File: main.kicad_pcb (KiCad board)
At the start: 2 copper layers, 228.6 x 70.6 mm, 133 parts, among them J1 Conn_02x16_Row_Letter_First, J10 Conn_01x26_Pin, J11 Conn_ARM_JTAG_SWD_10, J2 Conn_01x05, J3 Conn_01x02, J4 Screw_Terminal_01x02, J5 Screw_Terminal_01x10, J6 Screw_Terminal_01x10, J7 Screw_Terminal_01x02, J8 Screw_Terminal_01x10, J9 Screw_Terminal_01x10, U10 TLP3558A, U11 TLP3558A, U12 TLP3558A, U13 TLP3558A, U14 TLP3558A, U15 TLP3558A, U16 TLP3558A, U17 TLP3558A, U18 TLP3558A, U19 TLP3558A, U2 NCP1117-3.3_TO252, U20 TLP3558A, U21 TLP3558A, U22 TLP3558A, U23 TLP3558A, U24 TLP3558A, U25 TLP3558A, U26 TLP3558A, U27 TLP3558A, U28 TLP3558A, U29 TLP3558A, U3 STM32G070KBT6, U30 TLP3558A, U31 TLP3558A, U32 TLP3558A, U33 TLP3558A, U34 TLP3558A, U35 TLP3558A, U36 TLP3558A, U37 TLP3558A, U38 TLP3558A, U39 TLP3558A, U4 TLP3558A, U40 TLP3558A, U41 TLP3558A, U42 TLP3558A, U43 TLP3558A, U44 TLP3558A, U45 TLP3558A, U46 TLP3558A, U47 TLP3558A, U5 TLP3558A, U6 TLP3558A, U7 TLP3558A, U8 TLP3558A, U9 TLP3558A

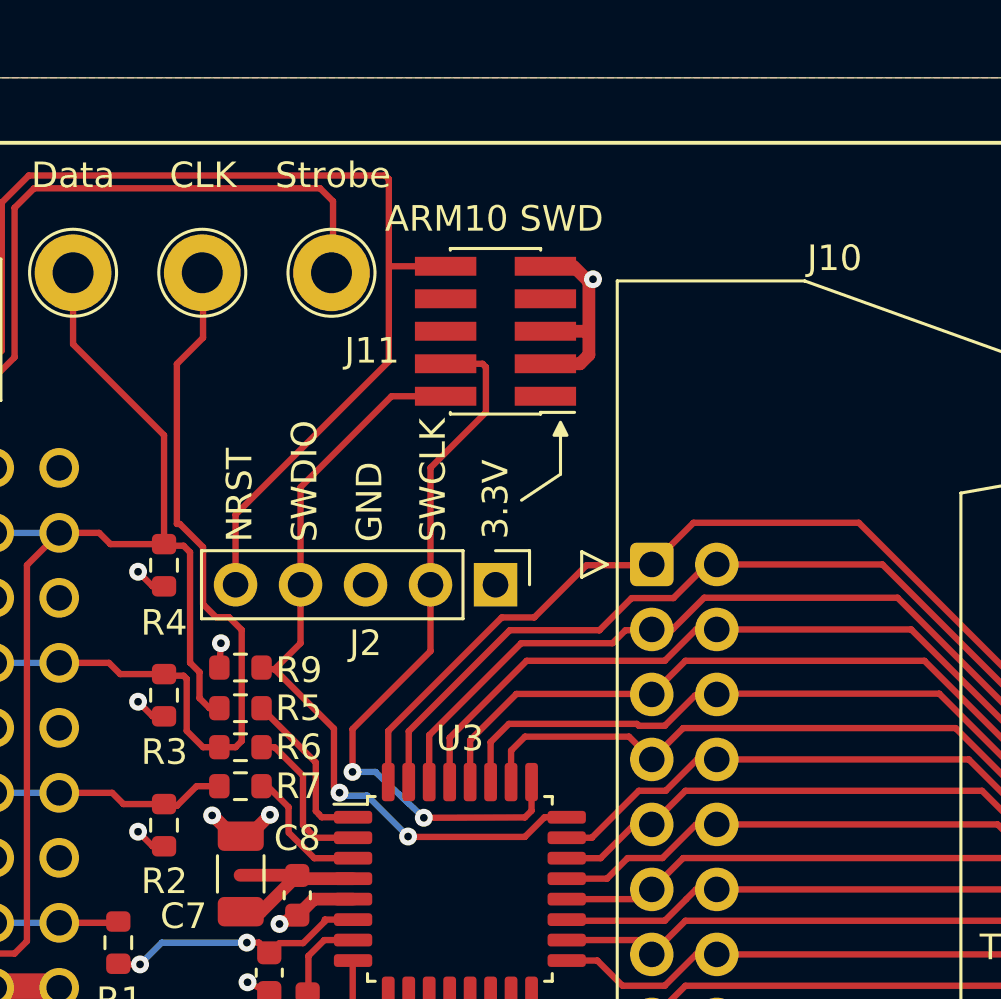
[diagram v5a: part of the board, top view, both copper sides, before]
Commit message: nicer SWD header
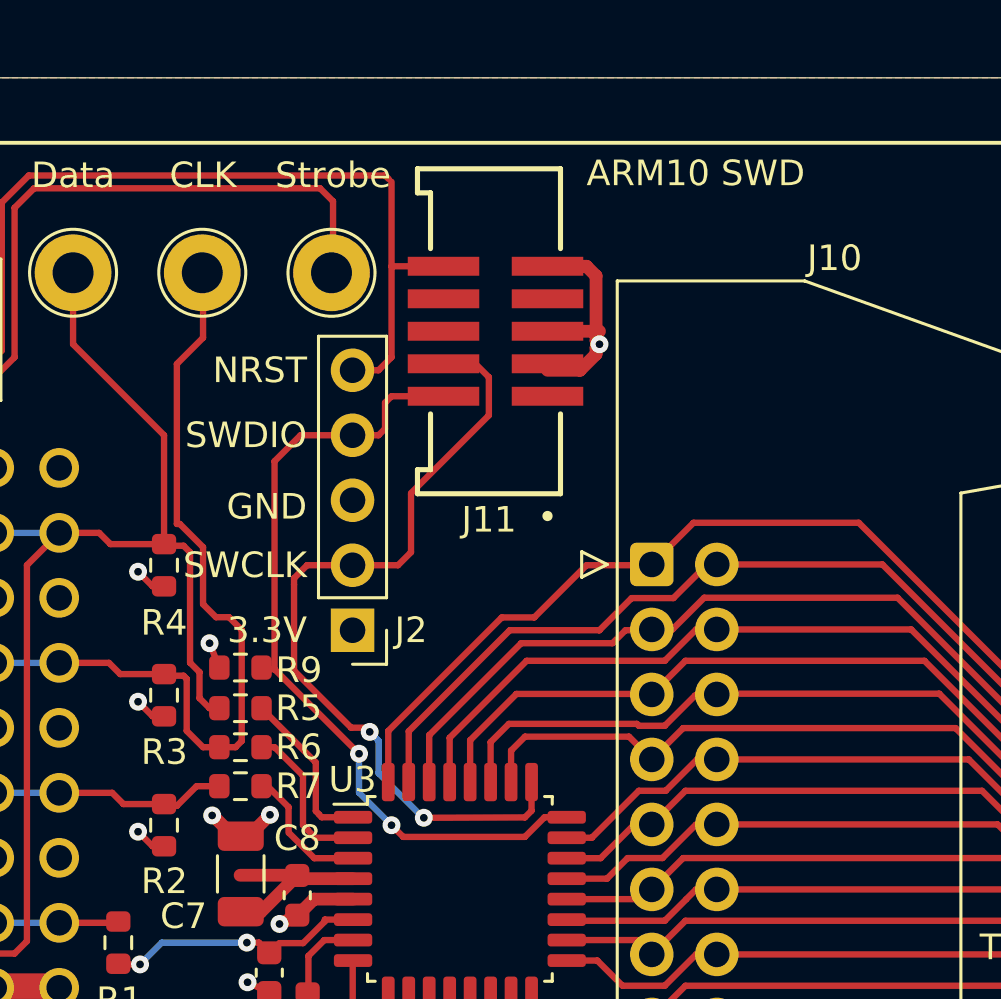
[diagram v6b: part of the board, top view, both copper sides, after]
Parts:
- J11: footprint Connector_PinHeader_1.27mm:PinHeader_2x05_P1.27mm_Vertical_SMD -> Custom_footprints_project:SAMTEC_SHF-105-01-L-D-SM-K-TR
- moved J2 5.86 mm to (44.7, 69.8), turned to 180 degrees
- turned J11 to 90 degrees
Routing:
- net /~{NRST}: track 70.2 -> 61.2 mm
- net /Microcontroller/SWCLK: track 28.6 -> 32.3 mm
- net GND: track 26.2 -> 28.4 mm

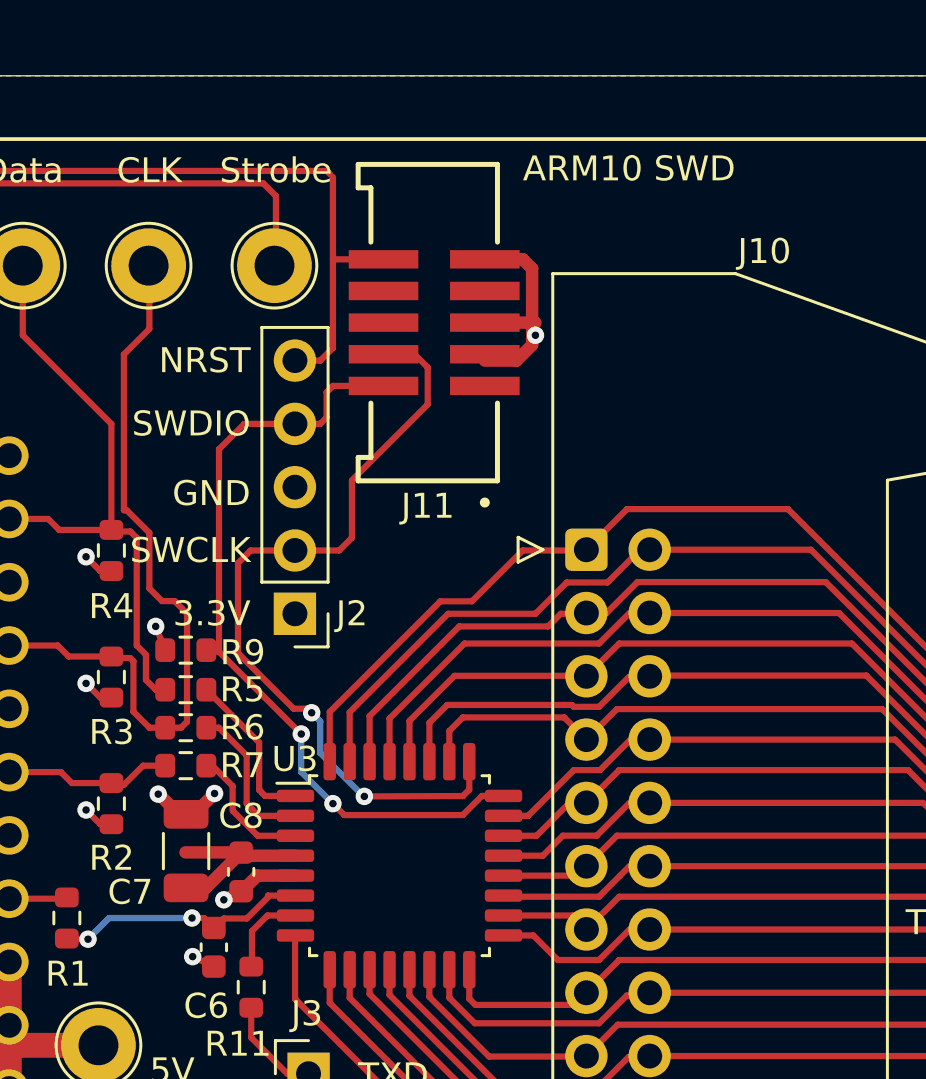
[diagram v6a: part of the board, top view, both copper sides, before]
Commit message: footprint of SWD connector more compatible
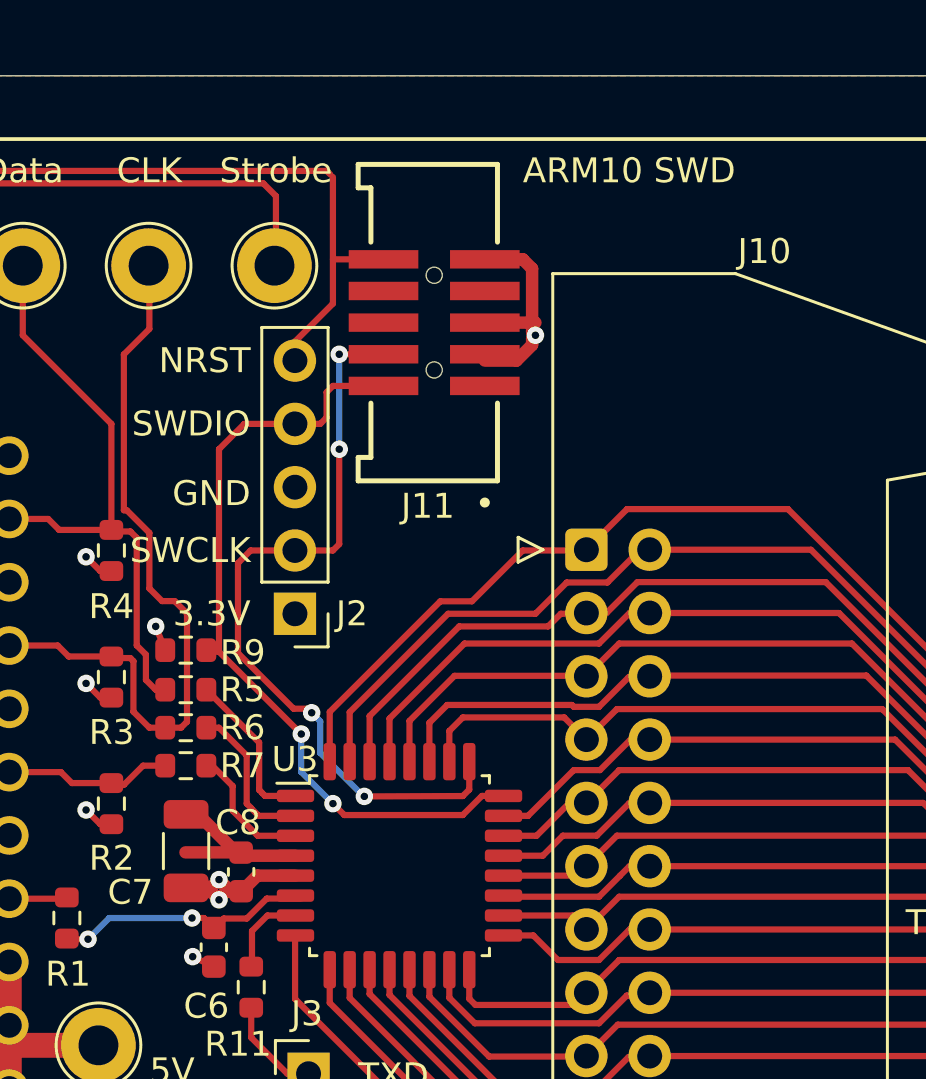
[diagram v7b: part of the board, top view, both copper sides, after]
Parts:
- turned C7 to -90 degrees
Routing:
- net GND: track 28.4 -> 30.3 mm, vias 13 -> 12
- net /~{NRST}: track 61.2 -> 60.6 mm
- net /Microcontroller/SWCLK: vias 2 -> 4

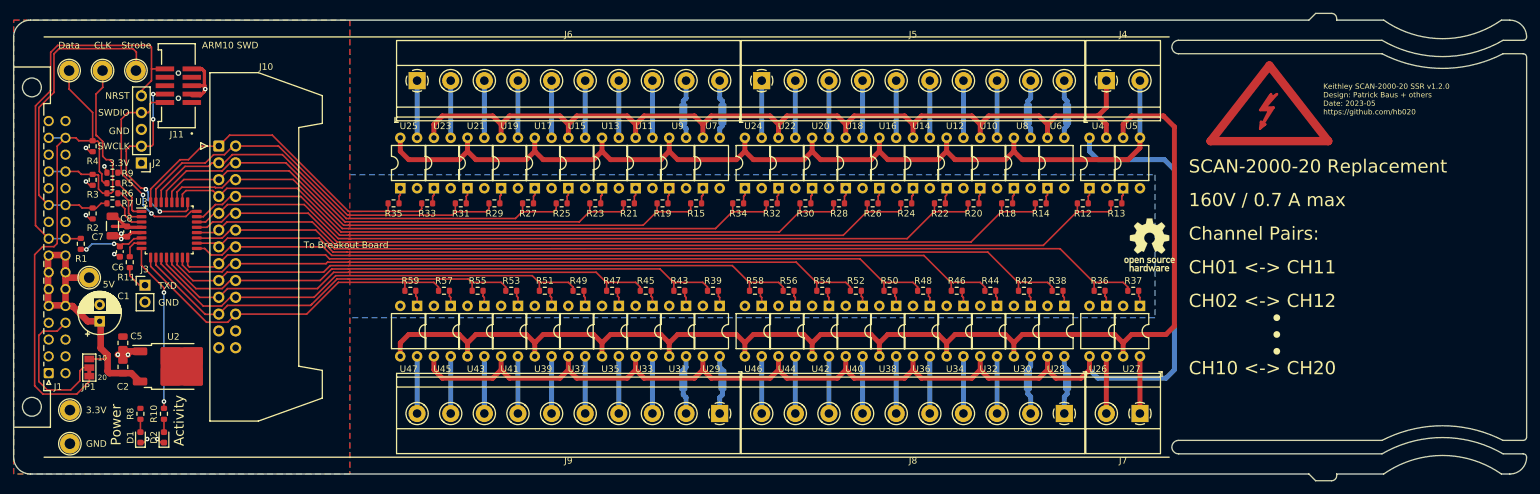
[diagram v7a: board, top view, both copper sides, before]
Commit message: improved silkscreen, better doc.
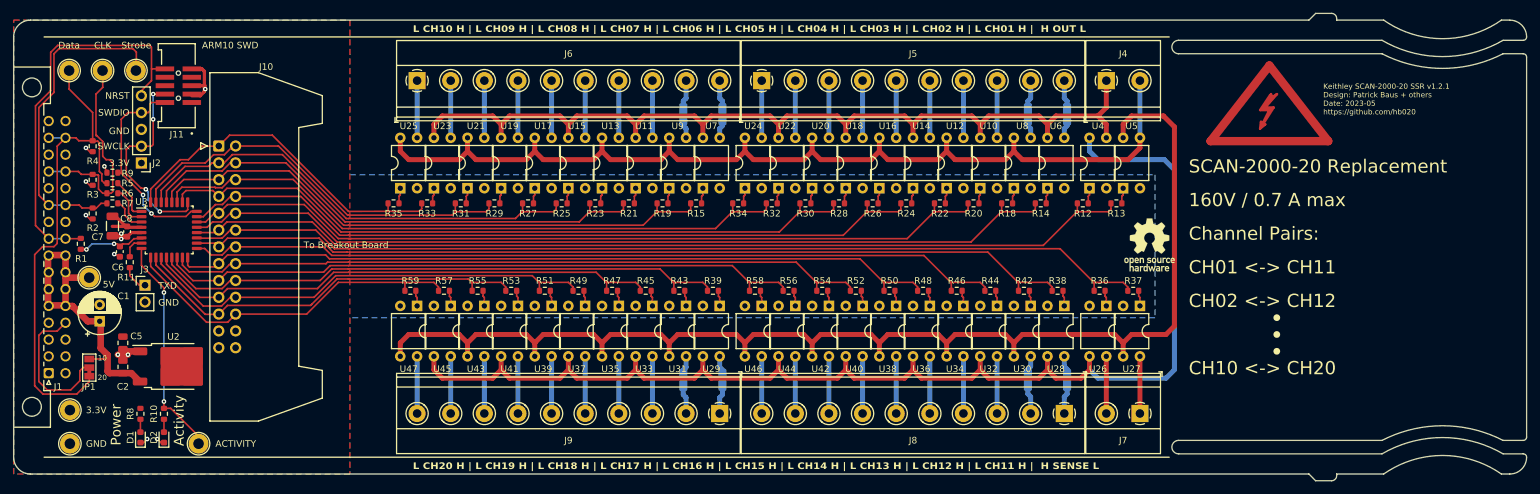
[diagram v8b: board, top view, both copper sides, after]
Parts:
- added TP7: TestPoint, TestPoint:TestPoint_Loop_D2.60mm_Drill1.6mm_Beaded, F.Cu at (53.3, 112.3)
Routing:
- net /Microcontroller/LED: track 25.6 -> 32.5 mm
- net /Microcontroller/SWCLK: track 32.3 -> 31.1 mm
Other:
- board text added: "ACTIVITY"
- board text added: "Keithley SCAN-2000-20 SSR v1.2.1 Design: Patrick Baus + others Date: 2023-05 https://github.com/hb020"
- board text added: "L CH10 H | L CH09 H | L CH08 H | L CH07 H | L CH06 H | L CH05 H | L CH04 H | L CH03 H | L CH02 H | L CH01 H | H OUT L"
- board text added: "L CH20 H | L CH19 H | L CH18 H | L CH17 H | L CH16 H | L CH15 H | L CH14 H | L CH13 H | L CH12 H | L CH11 H | H SENSE L"
- board text removed: "Keithley SCAN-2000-20 SSR v1.2.0 Design: Patrick Baus + others Date: 2023-05 https://github.com/hb020"
